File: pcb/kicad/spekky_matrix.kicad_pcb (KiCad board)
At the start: 2 copper layers, 153 x 95.8 mm, 330 parts, among them J1 USB_B_Micro, J2 Conn_ARM_JTAG_SWD_10, Q1 DMP3125L-7, Q2 DMP3125L-7, Q3 DMP3125L-7, Q4 DMP3125L-7, Q5 DMP3125L-7, Q6 DMP3125L-7, Q7 DMP3125L-7, Q8 DMP3125L-7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

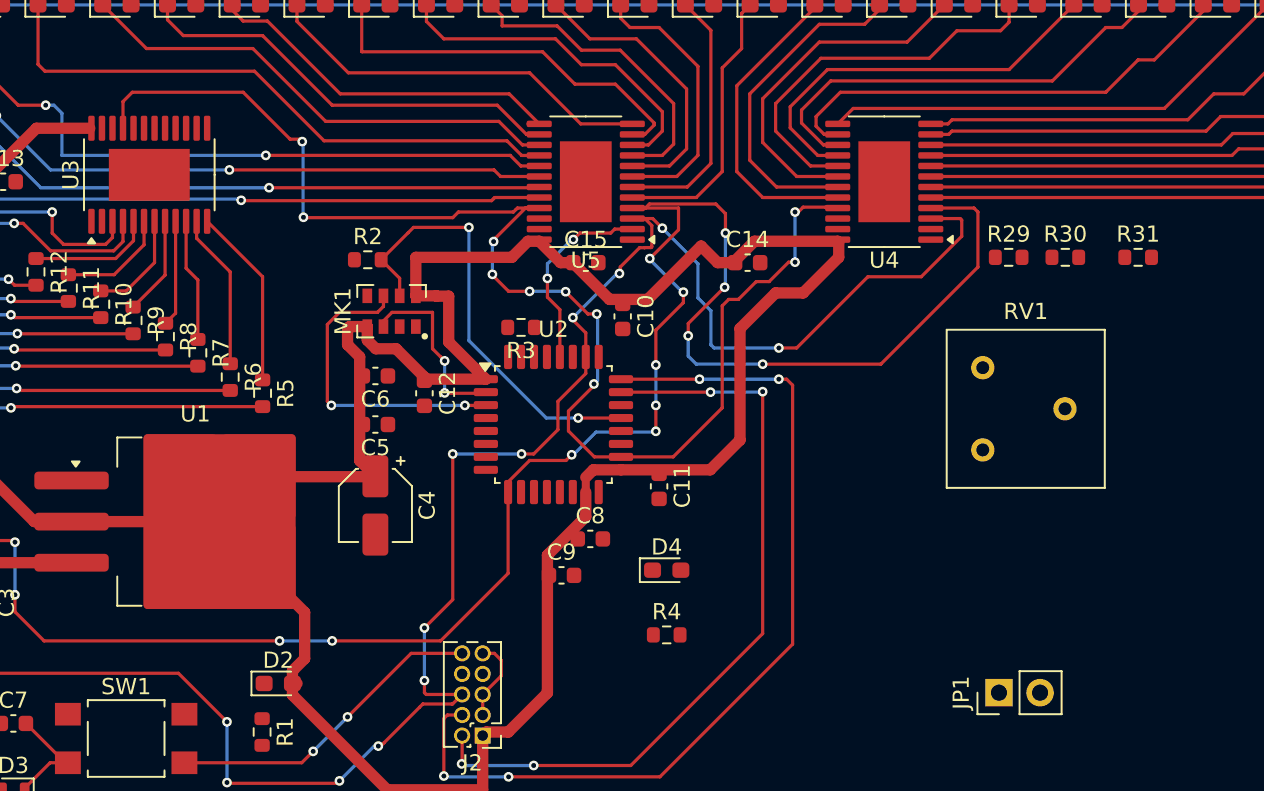
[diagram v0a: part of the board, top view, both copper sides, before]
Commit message: Connect potentiometer traces
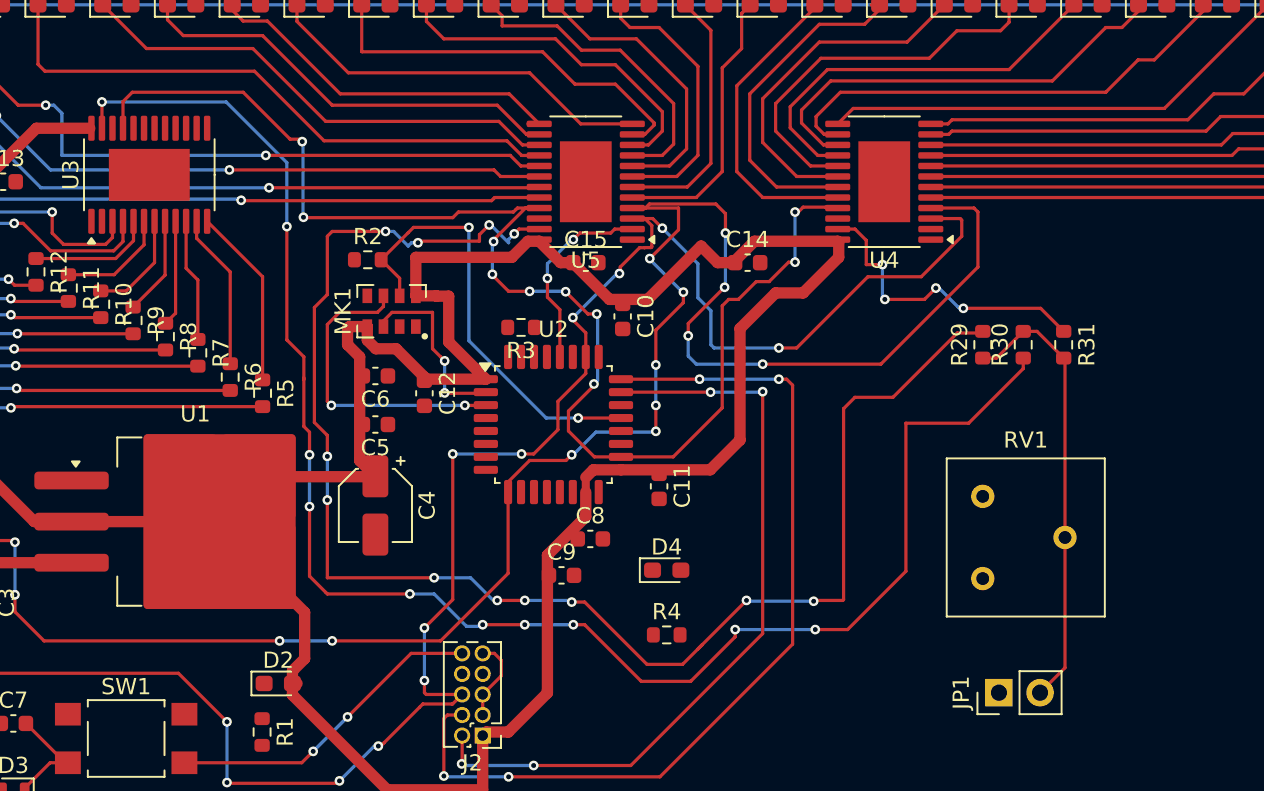
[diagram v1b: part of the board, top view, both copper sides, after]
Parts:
- moved RV1 7.95 mm to (146.5, 118.5)
- moved R31 7.09 mm to (151.5, 104.0), turned to -90 degrees
- moved R30 5.99 mm to (149.0, 104.0), turned to 90 degrees
- moved R29 5.63 mm to (146.5, 104.0), turned to 90 degrees
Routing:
- net /LED DRIVING/REXT3: track 0.00 -> 102.0 mm, vias 0 -> 10
- net /LED DRIVING/REXT1: track 0.00 -> 95.4 mm, vias 0 -> 12
- net Net-(JP1-B): track 0.00 -> 27.8 mm
- net /LED DRIVING/REXT2: track 0.00 -> 19.2 mm, vias 0 -> 4

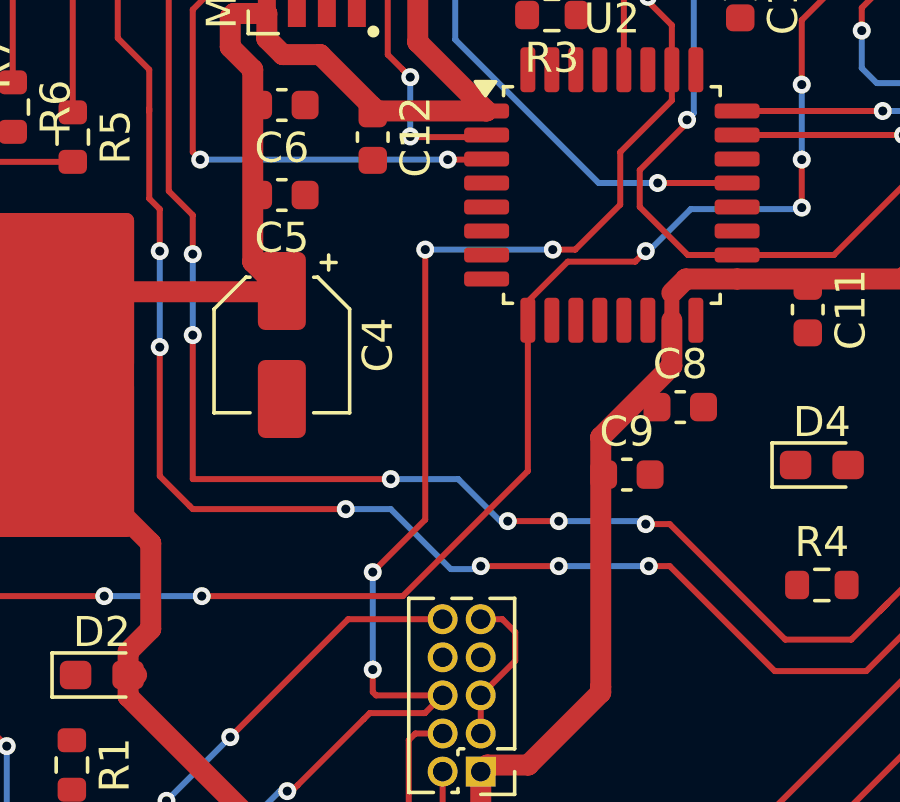
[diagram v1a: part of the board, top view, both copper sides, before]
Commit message: Connect nrst to stm32
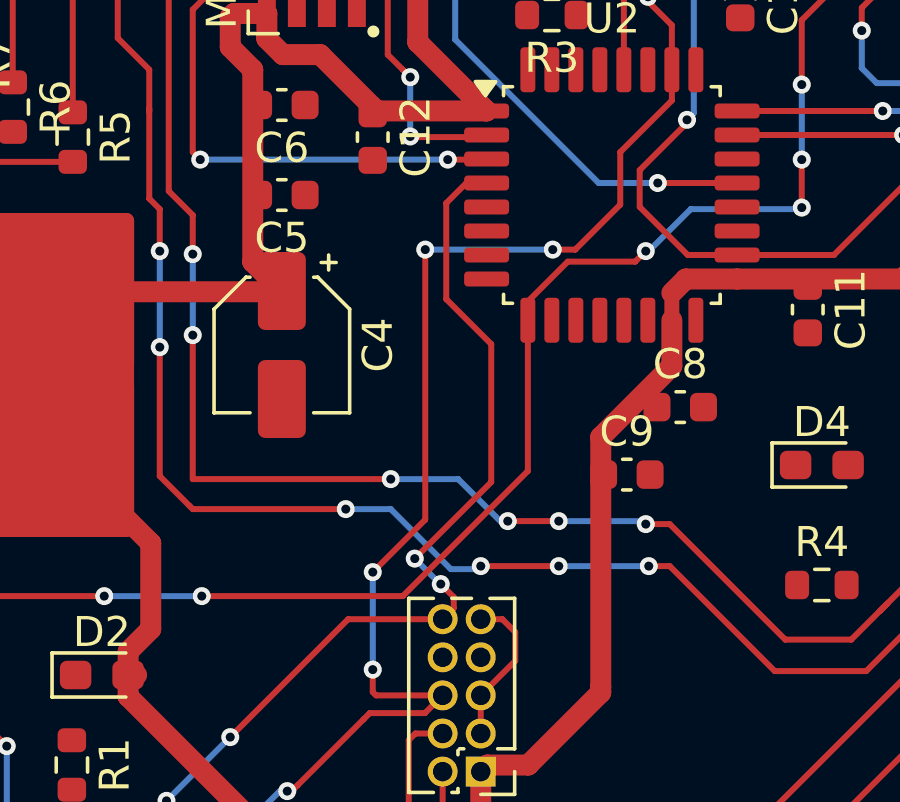
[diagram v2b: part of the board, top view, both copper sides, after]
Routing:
- net /STM32 MCU/NRST: track 26.9 -> 44.8 mm, vias 2 -> 4
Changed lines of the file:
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@@
+	)
+	(segment
+		(start 114.7 122.7)
+		(end 114.33 123.07)
+		(width 0.2)
+		(layer "F.Cu")
+		(net 5)
+	)
+	(segment
+		(start 115.120057 108.53)
+		(end 114.45 109.200057)
+		(width 0.2)
+		(layer "F.Cu")
+		(net 5)
 	)
 	(segment
@@
 	)
 	(segment
+		(start 115.95 113.9)
+		(end 115.95 118.5)
+		(width 0.2)
+		(layer "F.Cu")
+		(net 5)
+	)
+	(segment
+		(start 114.45 112.4)
+		(end 115.95 113.9)
+		(width 0.2)
+		(layer "F.Cu")
+		(net 5)
+	)
+	(segment
 		(start 88.87 129.83)
 		(end 87.3 131.4)
+		(width 0.2)
+		(layer "F.Cu")
+		(net 5)
+	)
+	(segment
+		(start 114.267179 121.899231)
+		(end 114.7 122.332052)
+		(width 0.2)
+		(layer "F.Cu")
+		(net 5)
+	)
+	(segment
+		(start 114.7 122.332052)
+		(end 114.7 122.7)
 		(width 0.2)
 		(layer "F.Cu")
@@
 	)
 	(segment
+		(start 115.795 108.53)
+		(end 115.120057 108.53)
+		(width 0.2)
+		(layer "F.Cu")
+		(net 5)
+	)
+	(segment
 		(start 105.125 129.125)
 		(end 104.42 129.83)
+		(width 0.2)
+		(layer "F.Cu")
+		(net 5)
+	)
+	(segment
+		(start 115.95 118.5)
+		(end 113.4 121.05)
+		(width 0.2)
+		(layer "F.Cu")
+		(net 5)
+	)
+	(segment
+		(start 114.45 109.200057)
+		(end 114.45 112.4)
 		(width 0.2)
 		(layer "F.Cu")
@@
 		(net 5)
 	)
+	(via
+		(at 114.267179 121.899231)
+		(size 0.6)
+		(drill 0.3)
+		(layers "F.Cu" "B.Cu")
+		(net 5)
+	)
+	(via
+		(at 113.4 121.05)
+		(size 0.6)
+		(drill 0.3)
+		(layers "F.Cu" "B.Cu")
+		(net 5)
+	)
 	(segment
 		(start 105.125 129.125)
@@
 		(width 0.2)
 		(layer "B.Cu")
+		(net 5)
+	)
+	(segment
+		(start 114.2 121.85)
+		(end 113.4 121.05)
+		(width 0.2)
+		(layer "B.Cu")
+		(net 5)
+	)
+	(segment
+		(start 114.267179 121.899231)
+		(end 114.217948 121.85)
+		(width 0.2)
+		(layer "B.Cu")
+		(net 5)
+	)
+	(segment
+		(start 114.217948 121.85)
+		(end 114.2 121.85)
+		(width 0.2)
+		(layer "B.Cu")

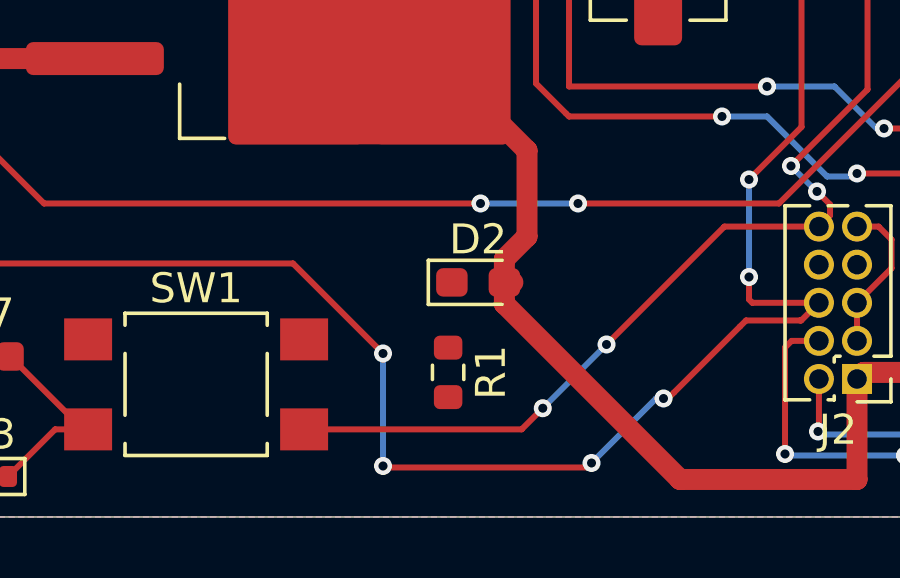
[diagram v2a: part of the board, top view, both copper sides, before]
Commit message: Connect 3v3 led indicator
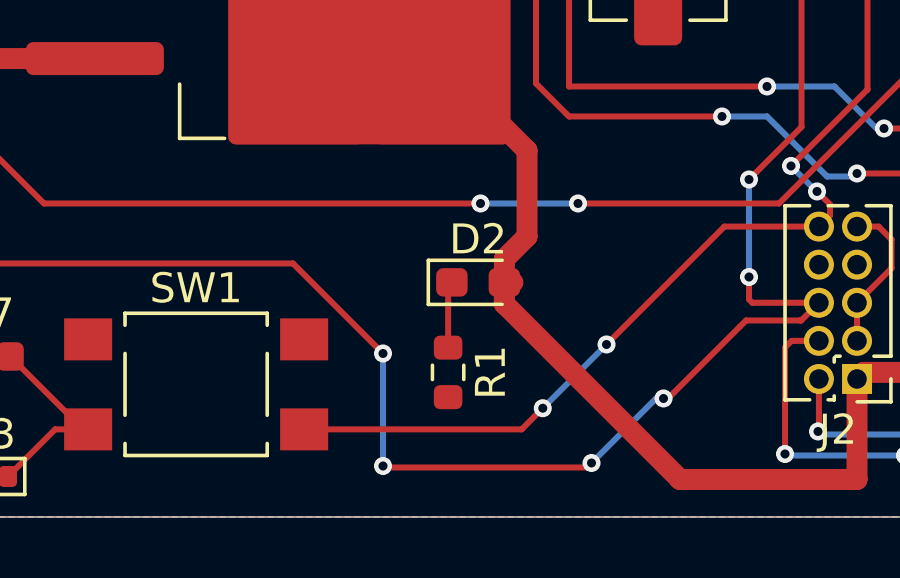
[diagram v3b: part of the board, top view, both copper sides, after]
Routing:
- net /POWER SHEET/3V3_PWR_LED_K: track 0.00 -> 2.23 mm
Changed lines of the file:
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@@
 		(net 96)
+	)
+	(segment
+		(start 101.97 125.055)
+		(end 102.095 124.93)
+		(width 0.2)
+		(layer "F.Cu")
+		(net 109)
+	)
+	(segment
+		(start 101.97 127.105)
+		(end 101.97 125.055)
+		(width 0.2)
+		(layer "F.Cu")
+		(net 109)
 	)
 	(zone

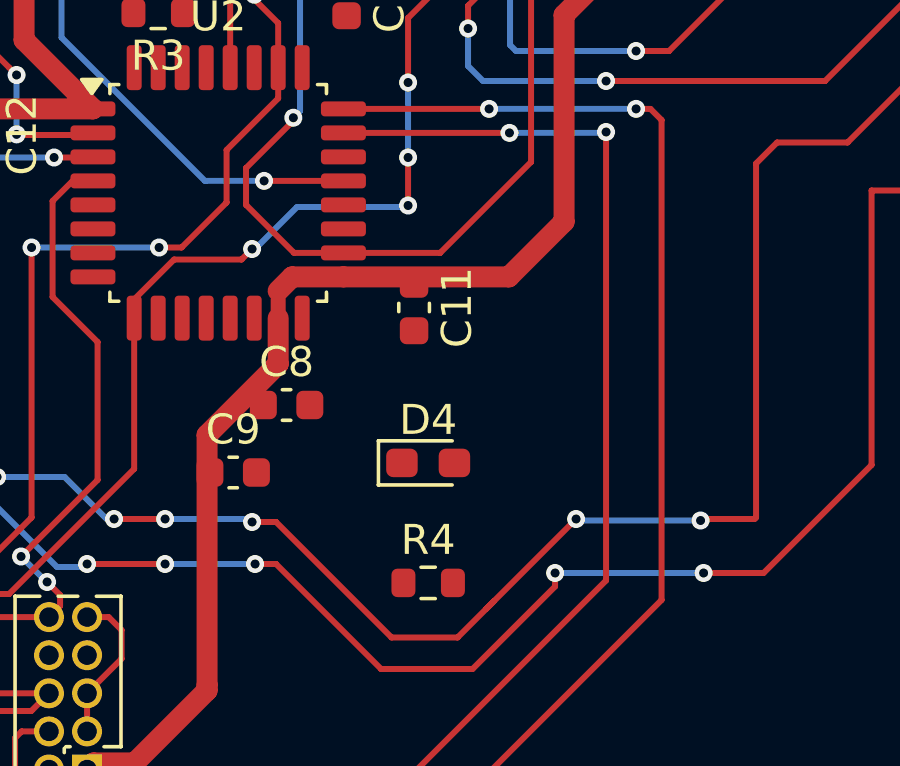
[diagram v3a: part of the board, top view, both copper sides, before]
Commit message: Connect gpio debug led
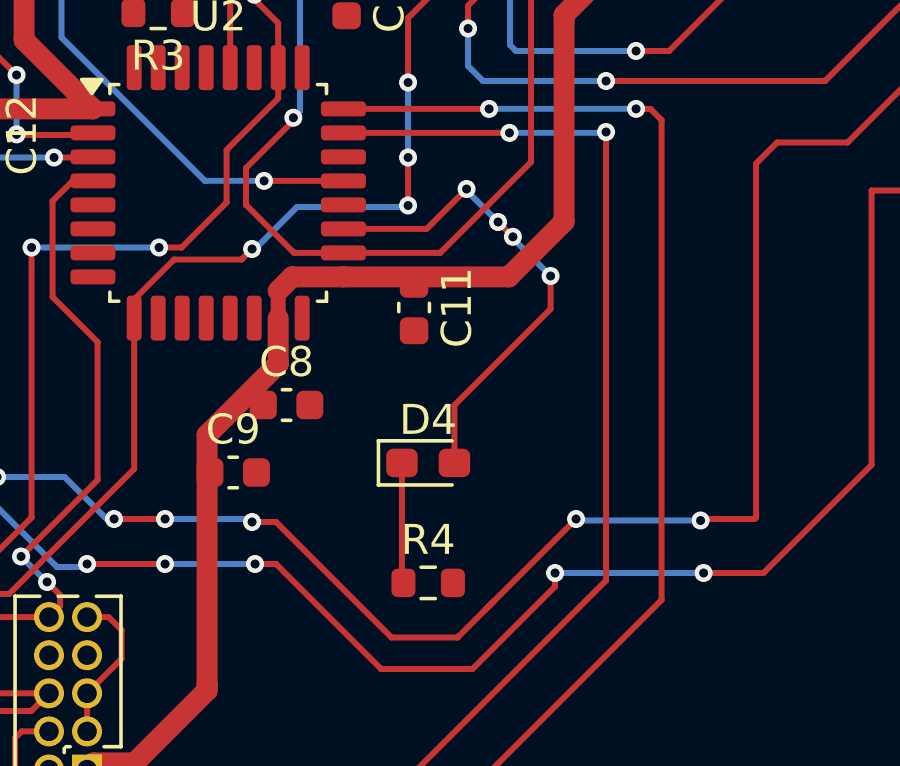
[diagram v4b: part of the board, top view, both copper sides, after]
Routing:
- net /STM32 MCU/GPIO_DEBUG1: track 0.00 -> 16.3 mm, vias 0 -> 4
- net Net-(D4-K): track 0.00 -> 4.02 mm
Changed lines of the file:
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@@
 	)
 	(segment
+		(start 129.3 109.9)
+		(end 129.793959 110.393959)
+		(width 0.2)
+		(layer "F.Cu")
+		(net 6)
+	)
+	(segment
+		(start 131.05 112.8)
+		(end 127.845 116.005)
+		(width 0.2)
+		(layer "F.Cu")
+		(net 6)
+	)
+	(segment
+		(start 124.145 110.13)
+		(end 126.92 110.13)
+		(width 0.2)
+		(layer "F.Cu")
+		(net 6)
+	)
+	(segment
+		(start 131.05 111.7)
+		(end 131.05 112.8)
+		(width 0.2)
+		(layer "F.Cu")
+		(net 6)
+	)
+	(segment
+		(start 126.92 110.13)
+		(end 127.1 109.95)
+		(width 0.2)
+		(layer "F.Cu")
+		(net 6)
+	)
+	(segment
+		(start 127.845 116.005)
+		(end 127.845 117.93)
+		(width 0.2)
+		(layer "F.Cu")
+		(net 6)
+	)
+	(segment
+		(start 127.1 109.95)
+		(end 128.25 108.8)
+		(width 0.2)
+		(layer "F.Cu")
+		(net 6)
+	)
+	(via
+		(at 129.793959 110.393959)
+		(size 0.6)
+		(drill 0.3)
+		(layers "F.Cu" "B.Cu")
+		(net 6)
+	)
+	(via
+		(at 129.3 109.9)
+		(size 0.6)
+		(drill 0.3)
+		(layers "F.Cu" "B.Cu")
+		(net 6)
+	)
+	(via
+		(at 131.05 111.7)
+		(size 0.6)
+		(drill 0.3)
+		(layers "F.Cu" "B.Cu")
+		(net 6)
+	)
+	(via
+		(at 128.25 108.8)
+		(size 0.6)
+		(drill 0.3)
+		(layers "F.Cu" "B.Cu")
+		(net 6)
+	)
+	(segment
+		(start 129.793959 110.443959)
+		(end 131.05 111.7)
+		(width 0.2)
+		(layer "B.Cu")
+		(net 6)
+	)
+	(segment
+		(start 128.25 108.8)
+		(end 128.25 108.85)
+		(width 0.2)
+		(layer "B.Cu")
+		(net 6)
+	)
+	(segment
+		(start 129.793959 110.393959)
+		(end 129.793959 110.443959)
+		(width 0.2)
+		(layer "B.Cu")
+		(net 6)
+	)
+	(segment
+		(start 128.25 108.85)
+		(end 129.3 109.9)
+		(width 0.2)
+		(layer "B.Cu")
+		(net 6)
+	)
+	(segment
 		(start 143.2875 94.905)
 		(end 184.22 94.905)
@@
 		(net 109)
 	)
+	(segment
+		(start 126.095 121.88)
+		(end 126.145 121.93)
+		(width 0.2)
+		(layer "F.Cu")
+		(net 110)
+	)
+	(segment
+		(start 126.095 117.93)
+		(end 126.095 121.88)
+		(width 0.2)
+		(layer "F.Cu")
+		(net 110)
+	)
 	(zone

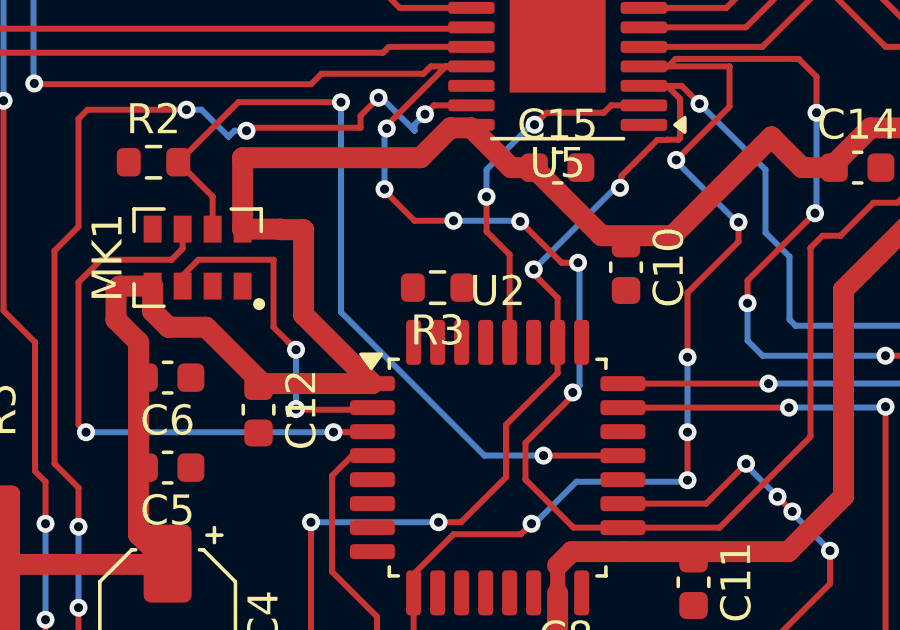
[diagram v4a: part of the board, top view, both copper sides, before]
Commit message: Connect pb8/boot0 resistor to stm32
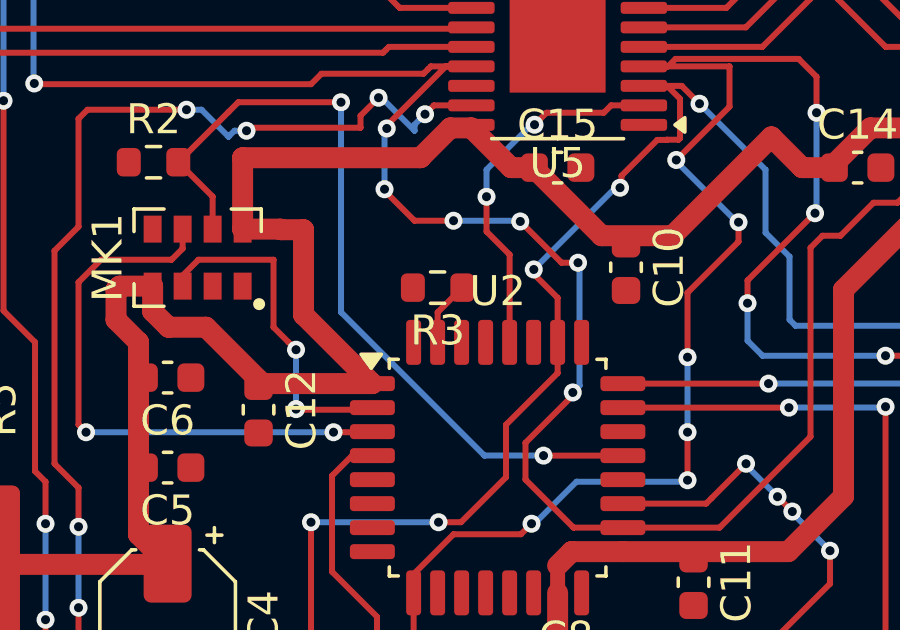
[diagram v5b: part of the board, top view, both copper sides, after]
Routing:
- net Net-(U2-PB8): track 0.00 -> 2.17 mm
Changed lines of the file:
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@@
+	)
+	(segment
+		(start 117.97 103.755)
+		(end 117.97 104.755)
+		(width 0.2)
+		(layer "F.Cu")
+		(net 68)
+	)
+	(segment
+		(start 118.795 102.93)
+		(end 117.97 103.755)
+		(width 0.2)
+		(layer "F.Cu")
+		(net 68)
 	)
 	(segment
